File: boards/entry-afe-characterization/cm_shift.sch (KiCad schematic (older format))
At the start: 0 parts

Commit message: Continued design of entry-afe-characterization
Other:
- note added: "TODO: single ended LMH6522 with +2 dB fixed gain\nand clipper circuit to keep output below 1.8V on both legs"
- note removed: "TODO: 8 dB single ended attenuator (0.398 V/V) on each leg"
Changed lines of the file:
@@
 GND
 Text Notes 3650 2500 0    50   ~ 0
-TODO: 8 dB single ended attenuator (0.398 V/V) on each leg
+TODO: single ended LMH6522 with +2 dB fixed gain\nand clipper circuit to keep output below 1.8V on both legs
 Text HLabel 4850 1750 2    50   Output ~ 0
 VOUT_P
 Text HLabel 4850 1850 2    50   Output ~ 0
 VOUT_N
+Text HLabel 3900 1900 0    50   Input ~ 0
+0V9_REF
 $EndSCHEMATC

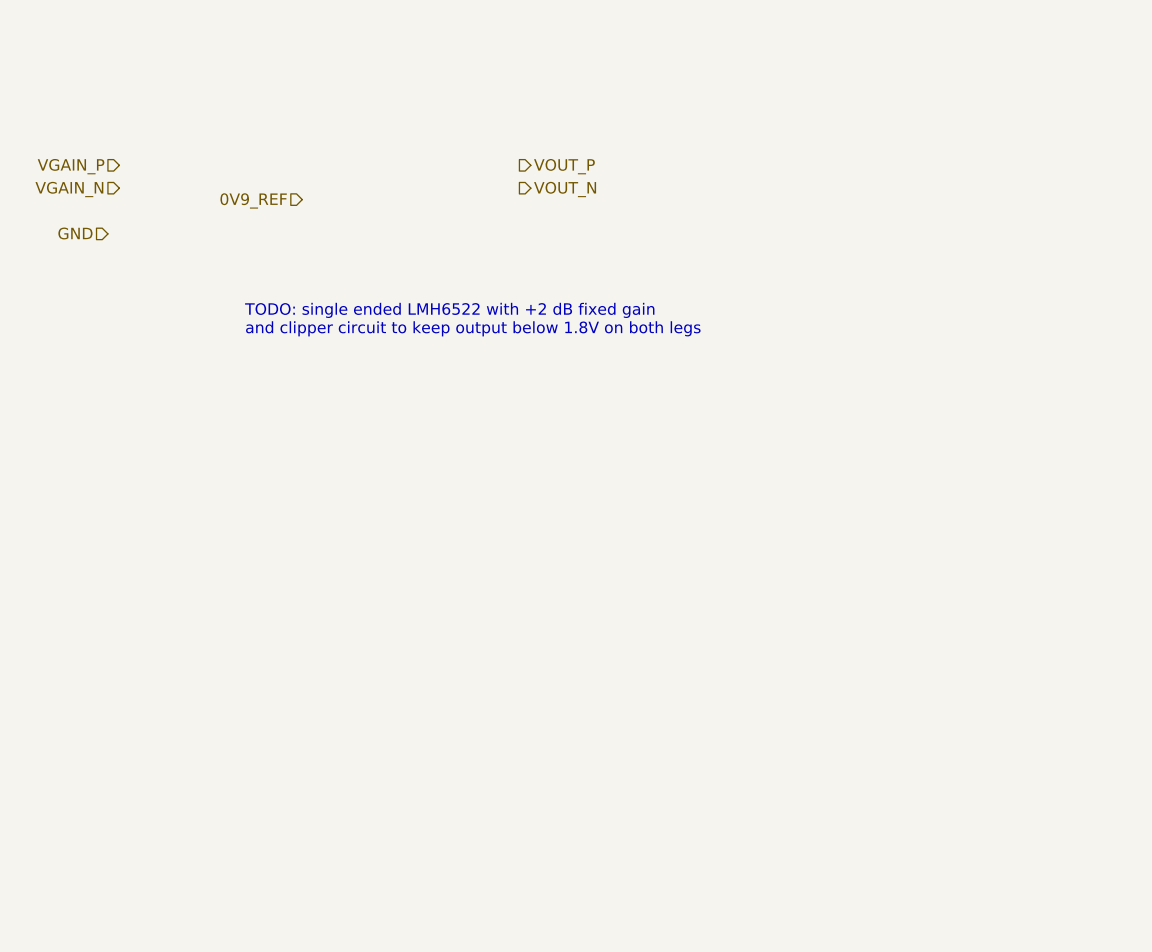
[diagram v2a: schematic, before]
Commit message: Continued work on AFE characterization board. Still have to do power supply.
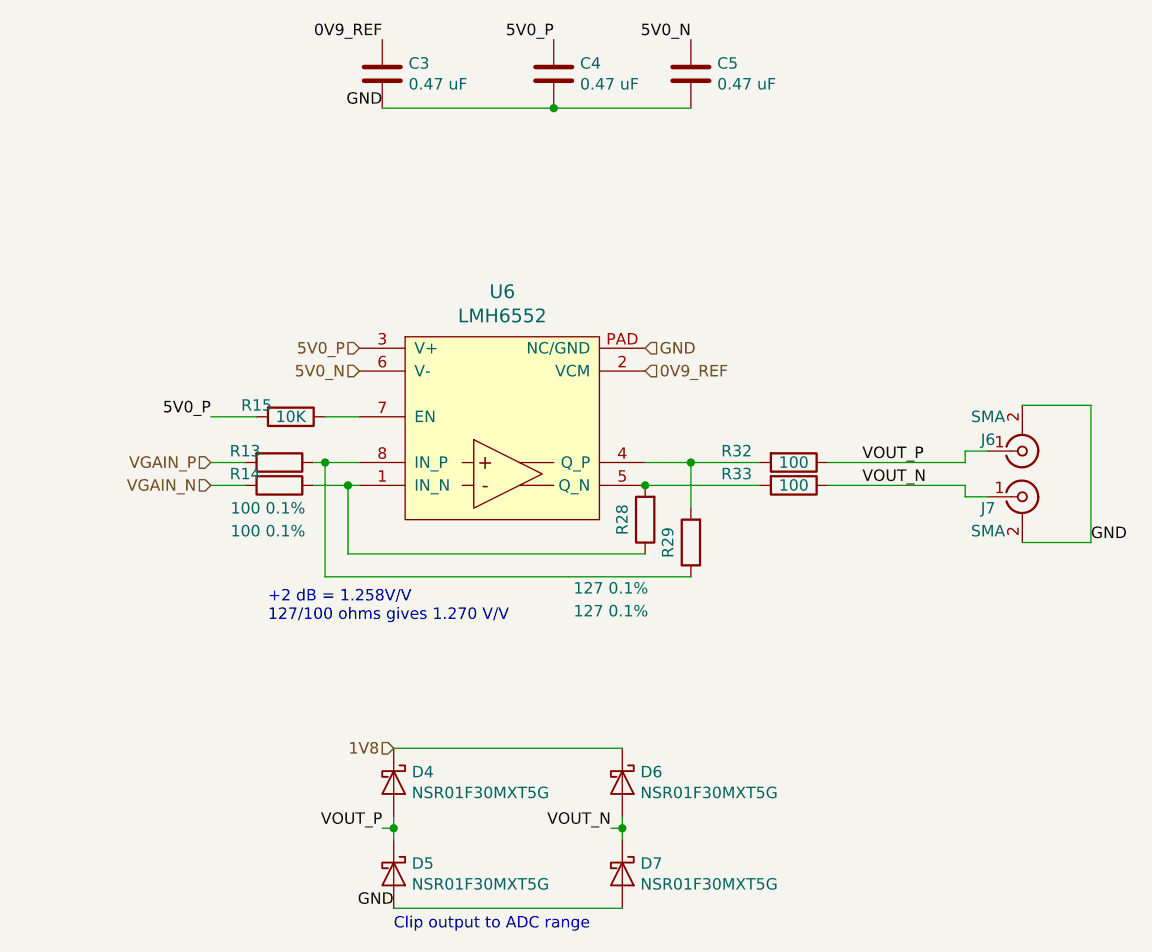
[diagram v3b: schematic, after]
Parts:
- added C3, C4, C5: 0.47 uF, symbol device:C
- added D4, D5, D6, D7: NSR01F30MXT5G, symbol device:D_Schottky
- added J6, J7: SMA, symbol Connector:Conn_Coaxial
- added R13, R14: 100 0.1%, symbol device:R
- added R15: 10K, symbol device:R
- added R28, R29: 127 0.1%, symbol device:R
- added R32, R33: 100, symbol device:R
- added U6: LMH6552, symbol analog-azonenberg:LMH6552
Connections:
- net 0V9_REF: now also C3.1, U6.2 (VCM)
- net GND: now also C3.2, C4.2, C5.2, D5.2 (A), D7.2 (A), J6.2 (Ext), J7.2 (Ext), U6.PAD (NC/GND)
- net VGAIN_N: now also R14.2
- net VGAIN_P: now also R13.2
- net VOUT_N: now also D6.2 (A), D7.1 (K), J7.1 (In), R33.1
- net VOUT_P: now also D4.2 (A), D5.1 (K), J6.1 (In), R32.1
- new net: R14.1, R28.1, U6.1 (IN_N)
- new net: R29.2, R32.2, U6.4 (Q_P)
- new net: R28.2, R33.2, U6.5 (Q_N)
- new net: R15.1, U6.7 (EN)
- new net: R13.1, R29.1, U6.8 (IN_P)
- new net 1V8: D4.1 (K), D6.1 (K)
- new net 5V0_N: C5.1, U6.6 (V-)
- new net 5V0_P: C4.1, R15.2, U6.3 (V+)
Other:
- note added: "+2 dB = 1.258V/V\n127/100 ohms gives 1.270 V/V"
- note added: "Clip output to ADC range"
- note removed: "TODO: single ended LMH6522 with +2 dB fixed gain\nand clipper circuit to keep output below 1.8V on both legs"

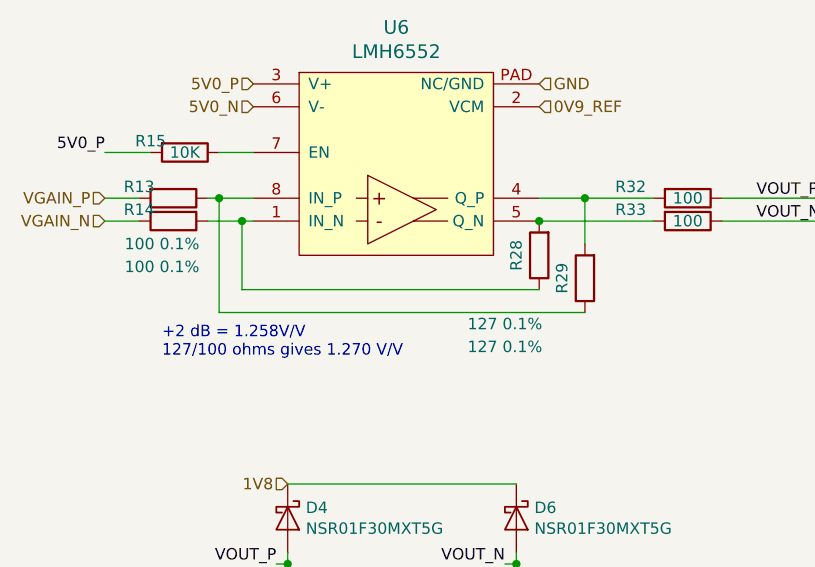
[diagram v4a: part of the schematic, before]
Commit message: Continued design review, added U18 to offset stage
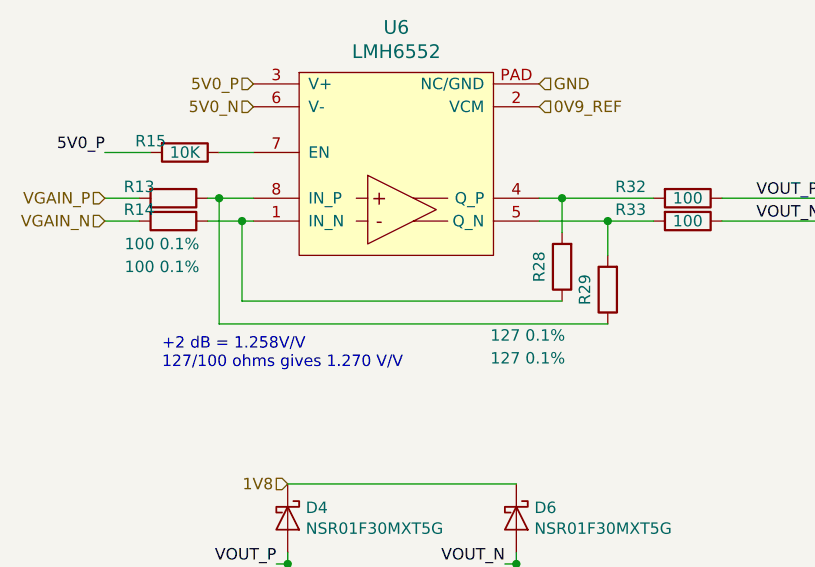
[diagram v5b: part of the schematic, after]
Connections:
- net at R32.2, U6.4 (Q_P): now also R28.2; no longer R29.2
- net at R33.2, U6.5 (Q_N): now also R29.2; no longer R28.2
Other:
- moved on the sheet: R28, R29
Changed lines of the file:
@@
 $Descr A4 11693 8268
 encoding utf-8
-Sheet 6 8
+Sheet 5 8
 Title "Entry-Level Oscilloscope AFE Characterization Platform"
-Date "2020-03-26"
+Date "2020-03-27"
 Rev "0.1"
 Comp "Antikernel Labs"
@@
 Wire Wire Line
 	3650 3150 3500 3150
-Wire Wire Line
-	3950 3050 4000 3050
-Wire Wire Line
-	3950 3150 4100 3150
 $Comp
 L device:R R28
 U 1 1 5E7B38B4
-P 5400 3300
-F 0 "R28" V 5500 3300 50  0000 C CNN
-F 1 "127 0.1%" H 5550 3600 50  0000 C CNN
-F 2 "" V 5330 3300 50  0001 C CNN
-F 3 "" H 5400 3300 50  0001 C CNN
-	1    5400 3300
+P 5500 3350
+F 0 "R28" V 5600 3350 50  0000 C CNN
+F 1 "127 0.1%" H 5650 3650 50  0000 C CNN
+F 2 "" V 5430 3350 50  0001 C CNN
+F 3 "" H 5500 3350 50  0001 C CNN
+	1    5500 3350
 	-1   0    0    1
 $EndComp
@@
 L device:R R29
 U 1 1 5E7B4812
-P 5600 3400
-F 0 "R29" V 5700 3400 50  0000 C CNN
-F 1 "127 0.1%" H 5950 3700 50  0000 C CNN
-F 2 "" V 5530 3400 50  0001 C CNN
-F 3 "" H 5600 3400 50  0001 C CNN
-	1    5600 3400
+P 5700 3450
+F 0 "R29" V 5800 3450 50  0000 C CNN
+F 1 "127 0.1%" H 6050 3750 50  0000 C CNN
+F 2 "" V 5630 3450 50  0001 C CNN
+F 3 "" H 5700 3450 50  0001 C CNN
+	1    5700 3450
 	-1   0    0    1
 $EndComp
-Wire Wire Line
-	5600 3250 5600 3050
-Wire Wire Line
-	5600 3050 5400 3050
-Wire Wire Line
-	5600 3550 4000 3550
-Wire Wire Line
-	4000 3550 4000 3050
-Connection ~ 4000 3050
-Wire Wire Line
-	4000 3050 4150 3050
-Wire Wire Line
-	5400 3450 4100 3450
-Wire Wire Line
-	4100 3450 4100 3150
-Connection ~ 4100 3150
-Wire Wire Line
-	4100 3150 4150 3150
 $Comp
 L device:R R15
@@
 Wire Wire Line
 	3500 2850 3700 2850
-Text Notes 3750 3750 0    50   ~ 0
+Text Notes 3750 3800 0    50   ~ 0
 +2 dB = 1.258V/V\n127/100 ohms gives 1.270 V/V
 Text HLabel 4300 4300 0    50   Input ~ 0
@@
 	0    1    1    0
 $EndComp
-Wire Wire Line
-	5900 3050 5600 3050
-Connection ~ 5600 3050
 $Comp
 L device:R R33
@@
 $EndComp
 Wire Wire Line
-	5400 3150 5900 3150
-Connection ~ 5400 3150
+	5400 3150 5700 3150
 Wire Wire Line
 	6200 3050 6800 3050
 Wire Wire Line
 	6800 3150 6200 3150
+Wire Wire Line
+	3950 3050 4000 3050
+Wire Wire Line
+	3950 3150 4100 3150
+Wire Wire Line
+	5400 3050 5500 3050
+Connection ~ 4000 3050
+Wire Wire Line
+	4000 3050 4150 3050
+Connection ~ 4100 3150
+Wire Wire Line
+	4100 3150 4150 3150
+Wire Wire Line
+	4100 3500 5500 3500
+Wire Wire Line
+	4100 3150 4100 3500
+Wire Wire Line
+	5500 3200 5500 3050
+Connection ~ 5500 3050
+Wire Wire Line
+	5500 3050 5900 3050
+Wire Wire Line
+	4000 3600 5700 3600
+Wire Wire Line
+	4000 3050 4000 3600
+Wire Wire Line
+	5700 3300 5700 3150
+Connection ~ 5700 3150
+Wire Wire Line
+	5700 3150 5900 3150
 $EndSCHEMATC

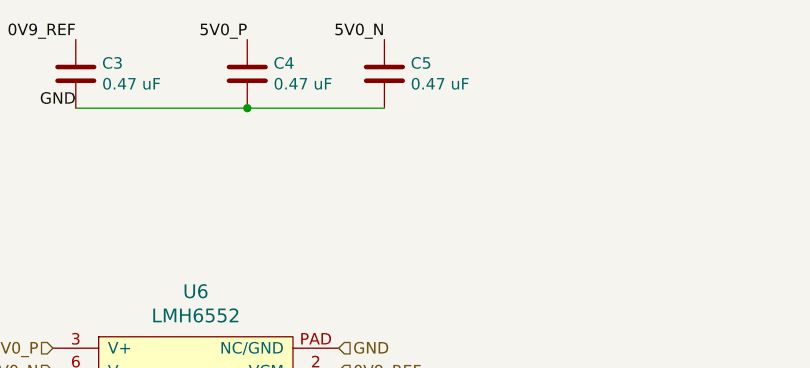
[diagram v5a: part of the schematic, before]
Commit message: Continued design review, began assigning footprints to sch symbols
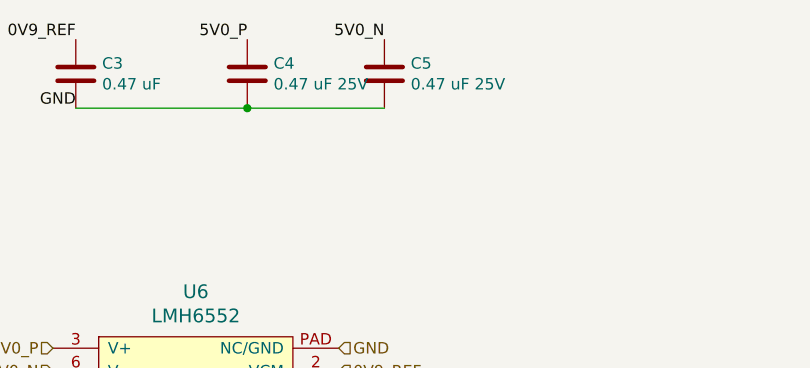
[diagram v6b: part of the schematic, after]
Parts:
- C3: footprint (none) -> azonenberg_pcb:EIA_0402_CAP_NOSILK
- C4, C5: value 0.47 uF -> 0.47 uF 25V; footprint (none) -> azonenberg_pcb:EIA_0402_CAP_NOSILK
- D4, D5, D6, D7: footprint (none) -> azonenberg_pcb:DFN_2_0.62x0.32
- J6, J7: footprint (none) -> azonenberg_pcb:CONN_SMA_EDGE_SAMTEC_SMA_J_P_H_ST_EM1
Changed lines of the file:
@@
 F 0 "U6" H 4775 4297 60  0000 C CNN
 F 1 "LMH6552" H 4775 4191 60  0000 C CNN
-F 2 "" H 3850 3250 60  0000 C CNN
+F 2 "" H 3850 3250 60  0001 C CNN
 F 3 "" H 3850 3250 60  0000 C CNN
 	1    4350 3300
@@
 F 0 "C3" H 4365 1396 50  0000 L CNN
 F 1 "0.47 uF" H 4365 1305 50  0000 L CNN
-F 2 "" H 4288 1200 50  0001 C CNN
+F 2 "azonenberg_pcb:EIA_0402_CAP_NOSILK" H 4288 1200 50  0001 C CNN
 F 3 "" H 4250 1350 50  0001 C CNN
 	1    4250 1350
@@
 P 5000 1350
 F 0 "C4" H 5115 1396 50  0000 L CNN
-F 1 "0.47 uF" H 5115 1305 50  0000 L CNN
-F 2 "" H 5038 1200 50  0001 C CNN
+F 1 "0.47 uF 25V" H 5115 1305 50  0000 L CNN
+F 2 "azonenberg_pcb:EIA_0402_CAP_NOSILK" H 5038 1200 50  0001 C CNN
 F 3 "" H 5000 1350 50  0001 C CNN
 	1    5000 1350
@@
 P 5600 1350
 F 0 "C5" H 5715 1396 50  0000 L CNN
-F 1 "0.47 uF" H 5715 1305 50  0000 L CNN
-F 2 "" H 5638 1200 50  0001 C CNN
+F 1 "0.47 uF 25V" H 5715 1305 50  0000 L CNN
+F 2 "azonenberg_pcb:EIA_0402_CAP_NOSILK" H 5638 1200 50  0001 C CNN
 F 3 "" H 5600 1350 50  0001 C CNN
 	1    5600 1350
@@
 F 0 "D5" V 4254 4929 50  0000 L CNN
 F 1 "NSR01F30MXT5G" V 4345 4929 50  0000 L CNN
-F 2 "" H 4300 4850 50  0001 C CNN
+F 2 "azonenberg_pcb:DFN_2_0.62x0.32" H 4300 4850 50  0001 C CNN
 F 3 "" H 4300 4850 50  0001 C CNN
 	1    4300 4850
@@
 F 0 "D4" V 4254 4529 50  0000 L CNN
 F 1 "NSR01F30MXT5G" V 4345 4529 50  0000 L CNN
-F 2 "" H 4300 4450 50  0001 C CNN
+F 2 "azonenberg_pcb:DFN_2_0.62x0.32" H 4300 4450 50  0001 C CNN
 F 3 "" H 4300 4450 50  0001 C CNN
 	1    4300 4450
@@
 F 0 "D6" V 5254 4529 50  0000 L CNN
 F 1 "NSR01F30MXT5G" V 5345 4529 50  0000 L CNN
-F 2 "" H 5300 4450 50  0001 C CNN
+F 2 "azonenberg_pcb:DFN_2_0.62x0.32" H 5300 4450 50  0001 C CNN
 F 3 "" H 5300 4450 50  0001 C CNN
 	1    5300 4450
@@
 F 0 "D7" V 5254 4929 50  0000 L CNN
 F 1 "NSR01F30MXT5G" V 5345 4929 50  0000 L CNN
-F 2 "" H 5300 4850 50  0001 C CNN
+F 2 "azonenberg_pcb:DFN_2_0.62x0.32" H 5300 4850 50  0001 C CNN
 F 3 "" H 5300 4850 50  0001 C CNN
 	1    5300 4850
@@
 F 0 "J6" H 6900 2950 50  0000 C CNN
 F 1 "SMA" H 6900 2850 50  0000 C CNN
-F 2 "" H 7050 3000 50  0001 C CNN
+F 2 "azonenberg_pcb:CONN_SMA_EDGE_SAMTEC_SMA_J_P_H_ST_EM1" H 7050 3000 50  0001 C CNN
 F 3 "" H 7050 3000 50  0001 C CNN
 	1    7050 3000
@@
 F 0 "J7" H 6900 3150 50  0000 C CNN
 F 1 "SMA" H 6900 3050 50  0000 C CNN
-F 2 "" H 7050 3200 50  0001 C CNN
+F 2 "azonenberg_pcb:CONN_SMA_EDGE_SAMTEC_SMA_J_P_H_ST_EM1" H 7050 3200 50  0001 C CNN
 F 3 "" H 7050 3200 50  0001 C CNN
 	1    7050 3200

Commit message: Continued assigning footprints
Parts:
- R13, R14, R15, R28, R29: footprint (none) -> azonenberg_pcb:EIA_0402_RES_NOSILK
- R32, R33: value 100 -> 49.9; footprint (none) -> azonenberg_pcb:EIA_0402_RES_NOSILK
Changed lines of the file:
@@
 F 0 "R13" V 3750 2900 50  0000 C CNN
 F 1 "100 0.1%" V 4000 3000 50  0000 C CNN
-F 2 "" V 3730 3050 50  0001 C CNN
+F 2 "azonenberg_pcb:EIA_0402_RES_NOSILK" V 3730 3050 50  0001 C CNN
 F 3 "" H 3800 3050 50  0001 C CNN
 	1    3800 3050
@@
 F 0 "R14" V 3750 3000 50  0000 C CNN
 F 1 "100 0.1%" V 4000 3100 50  0000 C CNN
-F 2 "" V 3730 3150 50  0001 C CNN
+F 2 "azonenberg_pcb:EIA_0402_RES_NOSILK" V 3730 3150 50  0001 C CNN
 F 3 "" H 3800 3150 50  0001 C CNN
 	1    3800 3150
@@
 F 0 "R28" V 5600 3350 50  0000 C CNN
 F 1 "127 0.1%" H 5650 3650 50  0000 C CNN
-F 2 "" V 5430 3350 50  0001 C CNN
+F 2 "azonenberg_pcb:EIA_0402_RES_NOSILK" V 5430 3350 50  0001 C CNN
 F 3 "" H 5500 3350 50  0001 C CNN
 	1    5500 3350
@@
 F 0 "R29" V 5800 3450 50  0000 C CNN
 F 1 "127 0.1%" H 6050 3750 50  0000 C CNN
-F 2 "" V 5630 3450 50  0001 C CNN
+F 2 "azonenberg_pcb:EIA_0402_RES_NOSILK" V 5630 3450 50  0001 C CNN
 F 3 "" H 5700 3450 50  0001 C CNN
 	1    5700 3450
@@
 F 0 "R15" V 3800 2700 50  0000 C CNN
 F 1 "10K" V 3850 2850 50  0000 C CNN
-F 2 "" V 3780 2850 50  0001 C CNN
+F 2 "azonenberg_pcb:EIA_0402_RES_NOSILK" V 3780 2850 50  0001 C CNN
 F 3 "" H 3850 2850 50  0001 C CNN
 	1    3850 2850
@@
 P 6050 3050
 F 0 "R32" V 6000 2800 50  0000 C CNN
-F 1 "100" V 6050 3050 50  0000 C CNN
-F 2 "" V 5980 3050 50  0001 C CNN
+F 1 "49.9" V 6050 3050 50  0000 C CNN
+F 2 "azonenberg_pcb:EIA_0402_RES_NOSILK" V 5980 3050 50  0001 C CNN
 F 3 "" H 6050 3050 50  0001 C CNN
 	1    6050 3050
@@
 P 6050 3150
 F 0 "R33" V 6000 2900 50  0000 C CNN
-F 1 "100" V 6050 3150 50  0000 C CNN
-F 2 "" V 5980 3150 50  0001 C CNN
+F 1 "49.9" V 6050 3150 50  0000 C CNN
+F 2 "azonenberg_pcb:EIA_0402_RES_NOSILK" V 5980 3150 50  0001 C CNN
 F 3 "" H 6050 3150 50  0001 C CNN
 	1    6050 3150

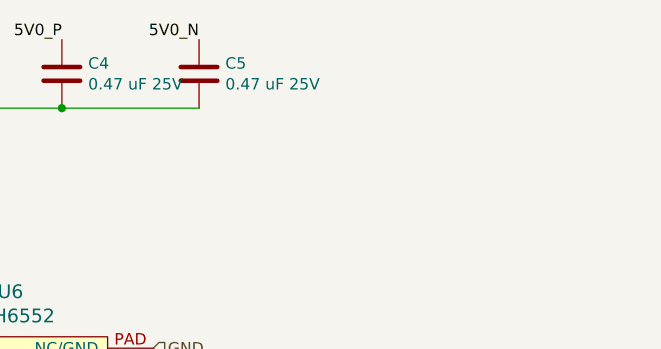
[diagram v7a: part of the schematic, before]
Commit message: Continued schematic review. Done with everything but test point/ground insertion.
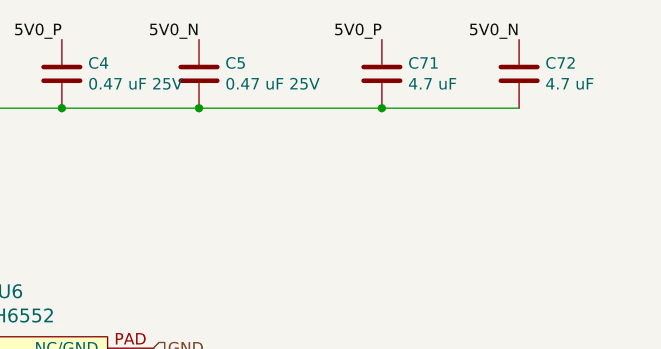
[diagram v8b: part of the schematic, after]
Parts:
- added C71, C72: 4.7 uF, azonenberg_pcb:EIA_0805_CAP_NOSILK, symbol device:C
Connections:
- net 5V0_N: now also C72.1
- net 5V0_P: now also C71.1
- net GND: now also C71.2, C72.2
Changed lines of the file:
@@
 Sheet 5 8
 Title "Entry-Level Oscilloscope AFE Characterization Platform"
-Date "2020-03-27"
+Date "2020-03-28"
 Rev "0.1"
 Comp "Antikernel Labs"
@@
 Wire Wire Line
 	5700 3150 5900 3150
+$Comp
+L device:C C?
+U 1 1 5EAA7EB6
+P 6400 1350
+AR Path="/5E73DF00/5EAA7EB6" Ref="C?"  Part="1"
+AR Path="/5E75B917/5EAA7EB6" Ref="C71"  Part="1"
+F 0 "C71" H 6515 1396 50  0000 L CNN
+F 1 "4.7 uF" H 6515 1305 50  0000 L CNN
+F 2 "azonenberg_pcb:EIA_0805_CAP_NOSILK" H 6438 1200 50  0001 C CNN
+F 3 "" H 6400 1350 50  0001 C CNN
+	1    6400 1350
+	1    0    0    -1
+$EndComp
+Wire Wire Line
+	5600 1500 6400 1500
+Connection ~ 5600 1500
+Text Label 6400 1200 2    50   ~ 0
+5V0_P
+$Comp
+L device:C C?
+U 1 1 5EAA8E3D
+P 7000 1350
+AR Path="/5E73DF00/5EAA8E3D" Ref="C?"  Part="1"
+AR Path="/5E75B917/5EAA8E3D" Ref="C72"  Part="1"
+F 0 "C72" H 7115 1396 50  0000 L CNN
+F 1 "4.7 uF" H 7115 1305 50  0000 L CNN
+F 2 "azonenberg_pcb:EIA_0805_CAP_NOSILK" H 7038 1200 50  0001 C CNN
+F 3 "" H 7000 1350 50  0001 C CNN
+	1    7000 1350
+	1    0    0    -1
+$EndComp
+Text Label 7000 1200 2    50   ~ 0
+5V0_N
+Wire Wire Line
+	7000 1500 6400 1500
+Connection ~ 6400 1500
 $EndSCHEMATC
